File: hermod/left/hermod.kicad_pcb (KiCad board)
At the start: 2 copper layers, 154 x 149.2 mm, 164 parts, among them J1 USB_C_Receptacle_USB2.0, J2 Conn_01x05, J3 USB_C_Receptacle_USB2.0, Q1 AO3401A, Q2 MMUN2233LT1G, U1 STM32F072CBT6, U2 PRTR5V0U2X, U3 XC6206PxxxMR-Regulator_Linear, U4 CR2013-MI2120, U5 TXB0101

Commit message: Finished routing
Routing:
- net GND: track 237.5 -> 233.0 mm
- net col0: track 243.0 -> 242.3 mm

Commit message: Updates
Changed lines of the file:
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@@
 		(fp_arc
 			(start 1.699999 -0.702844)
-			(mid 1.712537 -0.814067)
+			(mid 1.712538 -0.814067)
 			(end 1.749484 -0.919721)
 			(stroke
@@
 		(fp_arc
 			(start 1.749484 0.919719)
-			(mid 1.712534 0.814065)
+			(mid 1.712541 0.814065)
 			(end 1.699999 0.702841)
 			(stroke
@@
 		(fp_arc
 			(start 1.699999 -0.702844)
-			(mid 1.712537 -0.814068)
+			(mid 1.712536 -0.814067)
 			(end 1.749484 -0.919721)
 			(stroke
@@
 		(fp_arc
 			(start 1.749484 0.919719)
-			(mid 1.712517 0.81407)
+			(mid 1.712511 0.81407)
 			(end 1.699999 0.702841)
 			(stroke
@@
 		(fp_arc
 			(start 0.794452 1.499999)
-			(mid 0.925122 1.517375)
+			(mid 0.925123 1.517374)
 			(end 1.046711 1.568298)
 			(stroke
@@
 		(fp_arc
 			(start -1.046711 1.568296)
-			(mid -1.638069 1.504033)
+			(mid -1.638071 1.504032)
 			(end -1.749484 0.919719)
 			(stroke
@@
 		(fp_arc
 			(start 1.749484 0.919719)
-			(mid 1.712534 0.814065)
+			(mid 1.712541 0.814065)
 			(end 1.699999 0.702841)
 			(stroke
@@
 		(fp_arc
 			(start 1.699999 -0.702844)
-			(mid 1.712537 -0.814067)
+			(mid 1.712538 -0.814067)
 			(end 1.749484 -0.919721)
 			(stroke
@@
 		(fp_arc
 			(start 1.699999 -0.702844)
-			(mid 1.712537 -0.814067)
+			(mid 1.712538 -0.814067)
 			(end 1.749484 -0.919721)
 			(stroke
@@
 		(fp_arc
 			(start 1.749484 0.919719)
-			(mid 1.712534 0.814065)
+			(mid 1.712541 0.814065)
 			(end 1.699999 0.702841)
 			(stroke
@@
 		(fp_arc
 			(start 1.749484 0.919719)
-			(mid 1.712534 0.814065)
+			(mid 1.712541 0.814065)
 			(end 1.699999 0.702841)
 			(stroke
@@
 		(fp_arc
 			(start 1.699999 -0.702844)
-			(mid 1.712537 -0.814067)
+			(mid 1.712538 -0.814067)
 			(end 1.749484 -0.919721)
 			(stroke
@@
 		(fp_arc
 			(start 1.749484 0.919719)
-			(mid 1.712534 0.814065)
+			(mid 1.712541 0.814065)
 			(end 1.699999 0.702841)
 			(stroke
@@
 		(fp_arc
 			(start 1.699999 -0.702844)
-			(mid 1.712537 -0.814067)
+			(mid 1.712538 -0.814067)
 			(end 1.749484 -0.919721)
 			(stroke
@@
 		(fp_arc
 			(start 1.699999 -0.702844)
-			(mid 1.712537 -0.814067)
+			(mid 1.712538 -0.814067)
 			(end 1.749484 -0.919721)
 			(stroke
@@
 		(fp_arc
 			(start 1.749484 0.919719)
-			(mid 1.712534 0.814065)
+			(mid 1.712541 0.814065)
 			(end 1.699999 0.702841)
 			(stroke
@@
 		(fp_arc
 			(start 1.749484 0.919719)
-			(mid 1.712534 0.814065)
+			(mid 1.712541 0.814065)
 			(end 1.699999 0.702841)
 			(stroke
@@
 		(fp_arc
 			(start 1.699999 -0.702844)
-			(mid 1.712537 -0.814067)
+			(mid 1.712538 -0.814067)
 			(end 1.749484 -0.919721)
 			(stroke
@@
 		(fp_arc
 			(start 1.699999 -0.702844)
-			(mid 1.712537 -0.814067)
+			(mid 1.712538 -0.814067)
 			(end 1.749484 -0.919721)
 			(stroke
@@
 		(fp_arc
 			(start 1.749484 0.919719)
-			(mid 1.712534 0.814065)
+			(mid 1.712541 0.814065)
 			(end 1.699999 0.702841)
 			(stroke
@@
 		(fp_arc
 			(start 1.699999 -0.702844)
-			(mid 1.712537 -0.814068)
+			(mid 1.712536 -0.814067)
 			(end 1.749484 -0.919721)
 			(stroke
@@
 		(fp_arc
 			(start 1.749484 0.919719)
-			(mid 1.712517 0.81407)
+			(mid 1.712511 0.81407)
 			(end 1.699999 0.702841)
 			(stroke
@@
 		(fp_arc
 			(start 0.794452 1.499999)
-			(mid 0.925122 1.517375)
+			(mid 0.925123 1.517374)
 			(end 1.046711 1.568298)
 			(stroke
@@
 		(fp_arc
 			(start -1.046711 1.568296)
-			(mid -1.638069 1.504033)
+			(mid -1.638071 1.504032)
 			(end -1.749484 0.919719)
 			(stroke
@@
 		(fp_arc
 			(start 1.699999 -0.702844)
-			(mid 1.712537 -0.814067)
+			(mid 1.712538 -0.814067)
 			(end 1.749484 -0.919721)
 			(stroke
@@
 		(fp_arc
 			(start 1.749484 0.919719)
-			(mid 1.712534 0.814065)
+			(mid 1.712541 0.814065)
 			(end 1.699999 0.702841)
 			(stroke
@@
 		(fp_arc
 			(start 1.749484 0.919719)
-			(mid 1.712534 0.814065)
+			(mid 1.712541 0.814065)
 			(end 1.699999 0.702841)
 			(stroke
@@
 		(fp_arc
 			(start 1.699999 -0.702844)
-			(mid 1.712537 -0.814067)
+			(mid 1.712538 -0.814067)
 			(end 1.749484 -0.919721)
 			(stroke
@@
 		(fp_arc
 			(start 1.699999 -0.702844)
-			(mid 1.712537 -0.814067)
+			(mid 1.712538 -0.814067)
 			(end 1.749484 -0.919721)
 			(stroke
@@
 		(fp_arc
 			(start 1.749484 0.919719)
-			(mid 1.712534 0.814065)
+			(mid 1.712541 0.814065)
 			(end 1.699999 0.702841)
 			(stroke
@@
 		(fp_arc
 			(start 1.749484 0.919719)
-			(mid 1.712534 0.814065)
+			(mid 1.712541 0.814065)
 			(end 1.699999 0.702841)
 			(stroke
@@
 		(fp_arc
 			(start 1.699999 -0.702844)
-			(mid 1.712537 -0.814067)
+			(mid 1.712538 -0.814067)
 			(end 1.749484 -0.919721)
 			(stroke
@@
 		(fp_arc
 			(start 1.749484 0.919719)
-			(mid 1.712534 0.814065)
+			(mid 1.712541 0.814065)
 			(end 1.699999 0.702841)
 			(stroke
@@
 		(fp_arc
 			(start 1.699999 -0.702844)
-			(mid 1.712537 -0.814067)
+			(mid 1.712538 -0.814067)
 			(end 1.749484 -0.919721)
 			(stroke
@@
 		(fp_arc
 			(start 1.699999 -0.702844)
-			(mid 1.712537 -0.814067)
+			(mid 1.712538 -0.814067)
 			(end 1.749484 -0.919721)
 			(stroke
@@
 		(fp_arc
 			(start 1.749484 0.919719)
-			(mid 1.712534 0.814065)
+			(mid 1.712541 0.814065)
 			(end 1.699999 0.702841)
 			(stroke
@@
 		(fp_arc
 			(start 1.699999 -0.702844)
-			(mid 1.712537 -0.814067)
+			(mid 1.712538 -0.814067)
 			(end 1.749484 -0.919721)
 			(stroke
@@
 		(fp_arc
 			(start 1.749484 0.919719)
-			(mid 1.712534 0.814065)
+			(mid 1.712541 0.814065)
 			(end 1.699999 0.702841)
 			(stroke
@@
 		(fp_arc
 			(start 1.699999 -0.702844)
-			(mid 1.712537 -0.814067)
+			(mid 1.712538 -0.814067)
 			(end 1.749484 -0.919721)
 			(stroke
@@
 		(fp_arc
 			(start 1.749484 0.919719)
-			(mid 1.712534 0.814065)
+			(mid 1.712541 0.814065)
 			(end 1.699999 0.702841)
 			(stroke
@@
 		(fp_arc
 			(start 1.699999 -0.702844)
-			(mid 1.712537 -0.814067)
+			(mid 1.712538 -0.814067)
 			(end 1.749484 -0.919721)
 			(stroke
@@
 		(fp_arc
 			(start 1.749484 0.919719)
-			(mid 1.712534 0.814065)
+			(mid 1.712541 0.814065)
 			(end 1.699999 0.702841)
 			(stroke
@@
 		(fp_arc
 			(start 1.699999 -0.702844)
-			(mid 1.712537 -0.814067)
+			(mid 1.712538 -0.814067)
 			(end 1.749484 -0.919721)
 			(stroke
@@
 		(fp_arc
 			(start 1.749484 0.919719)
-			(mid 1.712534 0.814065)
+			(mid 1.712541 0.814065)
 			(end 1.699999 0.702841)
 			(stroke
@@
 		(fp_arc
 			(start 1.699999 -0.702844)
-			(mid 1.712537 -0.814067)
+			(mid 1.712538 -0.814067)
 			(end 1.749484 -0.919721)
 			(stroke
@@
 		(fp_arc
 			(start 1.749484 0.919719)
-			(mid 1.712534 0.814065)
+			(mid 1.712541 0.814065)
 			(end 1.699999 0.702841)
 			(stroke
@@
 		(fp_arc
 			(start 1.699999 -0.702844)
-			(mid 1.712537 -0.814067)
+			(mid 1.712538 -0.814067)
 			(end 1.749484 -0.919721)
 			(stroke
@@
 		(fp_arc
 			(start 1.749484 0.919719)
-			(mid 1.712534 0.814065)
+			(mid 1.712541 0.814065)
 			(end 1.699999 0.702841)
 			(stroke
@@
 		(fp_arc
 			(start 1.749484 0.919719)
-			(mid 1.712534 0.814065)
+			(mid 1.712541 0.814065)
 			(end 1.699999 0.702841)
 			(stroke
@@
 		(fp_arc
 			(start 1.699999 -0.702844)
-			(mid 1.712537 -0.814067)
+			(mid 1.712538 -0.814067)
 			(end 1.749484 -0.919721)
 			(stroke
@@
 		(fp_arc
 			(start 1.699999 -0.702844)
-			(mid 1.712537 -0.814067)
+			(mid 1.712538 -0.814067)
 			(end 1.749484 -0.919721)
 			(stroke
@@
 		(fp_arc
 			(start 1.749484 0.919719)
-			(mid 1.712534 0.814065)
+			(mid 1.712541 0.814065)
 			(end 1.699999 0.702841)
 			(stroke
@@
 		(fp_arc
 			(start 1.699999 -0.702844)
-			(mid 1.712537 -0.814067)
+			(mid 1.712538 -0.814067)
 			(end 1.749484 -0.919721)
 			(stroke
@@
 		(fp_arc
 			(start 1.749484 0.919719)
-			(mid 1.712534 0.814065)
+			(mid 1.712541 0.814065)
 			(end 1.699999 0.702841)
 			(stroke
@@
 		(fp_arc
 			(start 1.699999 -0.702844)
-			(mid 1.712537 -0.814067)
+			(mid 1.712538 -0.814067)
 			(end 1.749484 -0.919721)
 			(stroke
@@
 		(fp_arc
 			(start 1.749484 0.919719)
-			(mid 1.712534 0.814065)
+			(mid 1.712541 0.814065)
 			(end 1.699999 0.702841)
 			(stroke
@@
 		(fp_arc
 			(start 1.699999 -0.702844)
-			(mid 1.712537 -0.814067)
+			(mid 1.712538 -0.814067)
 			(end 1.749484 -0.919721)
 			(stroke
@@
 		(fp_arc
 			(start 1.749484 0.919719)
-			(mid 1.712534 0.814065)
+			(mid 1.712541 0.814065)
 			(end 1.699999 0.702841)
 			(stroke
@@
 		(fp_arc
 			(start 1.749484 0.919719)
-			(mid 1.712534 0.814065)
+			(mid 1.712541 0.814065)
 			(end 1.699999 0.702841)
 			(stroke
@@
 		(fp_arc
 			(start 1.699999 -0.702844)
-			(mid 1.712537 -0.814067)
+			(mid 1.712538 -0.814067)
 			(end 1.749484 -0.919721)
 			(stroke
@@
 		(fp_arc
 			(start 1.749484 0.919719)
-			(mid 1.712534 0.814065)
+			(mid 1.712541 0.814065)
 			(end 1.699999 0.702841)
 			(stroke
@@
 		(fp_arc
 			(start 1.699999 -0.702844)
-			(mid 1.712537 -0.814067)
+			(mid 1.712538 -0.814067)
 			(end 1.749484 -0.919721)
 			(stroke
@@
 		(fp_arc
 			(start 1.699999 -0.702844)
-			(mid 1.712537 -0.814067)
+			(mid 1.712538 -0.814067)
 			(end 1.749484 -0.919721)
 			(stroke
@@
 		(fp_arc
 			(start 1.749484 0.919719)
-			(mid 1.712534 0.814065)
+			(mid 1.712541 0.814065)
 			(end 1.699999 0.702841)
 			(stroke
@@
 		(fp_arc
 			(start 1.749484 0.919719)
-			(mid 1.712534 0.814065)
+			(mid 1.712541 0.814065)
 			(end 1.699999 0.702841)
 			(stroke
@@
 		(fp_arc
 			(start 1.699999 -0.702844)
-			(mid 1.712537 -0.814067)
+			(mid 1.712538 -0.814067)
 			(end 1.749484 -0.919721)
 			(stroke
@@
 		(fp_arc
 			(start 1.749484 0.919719)
-			(mid 1.712534 0.814065)
+			(mid 1.712541 0.814065)
 			(end 1.699999 0.702841)
 			(stroke
@@
 		(fp_arc
 			(start 1.699999 -0.702844)
-			(mid 1.712537 -0.814067)
+			(mid 1.712538 -0.814067)
 			(end 1.749484 -0.919721)
 			(stroke

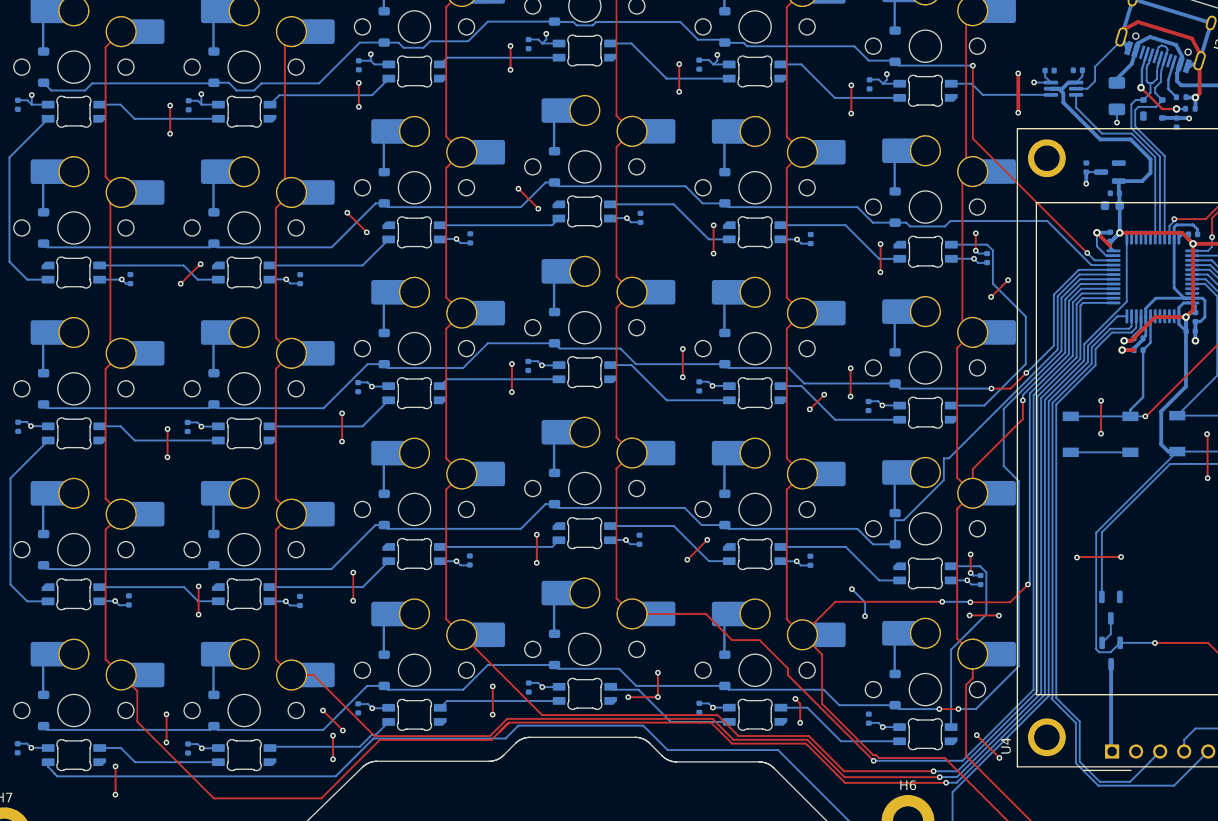
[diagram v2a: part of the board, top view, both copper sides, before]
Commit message: Added PCBWay DRC presets
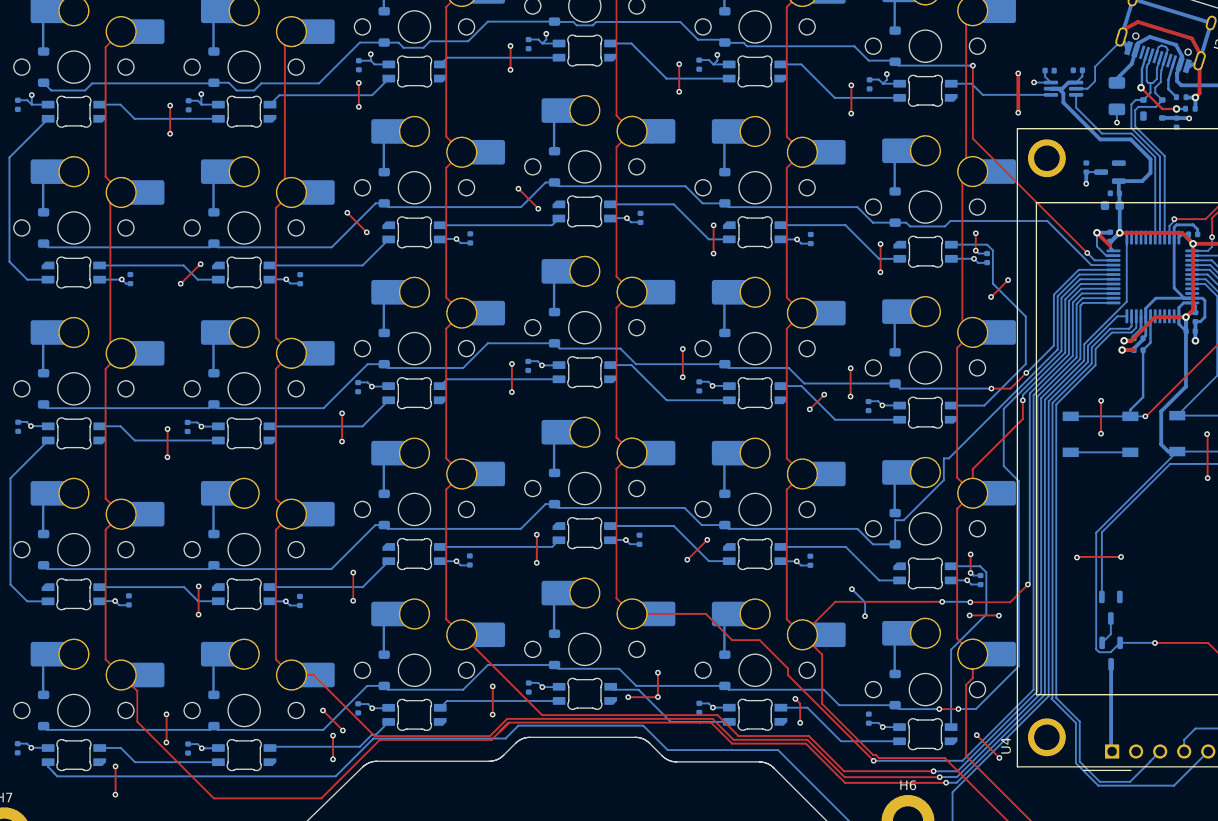
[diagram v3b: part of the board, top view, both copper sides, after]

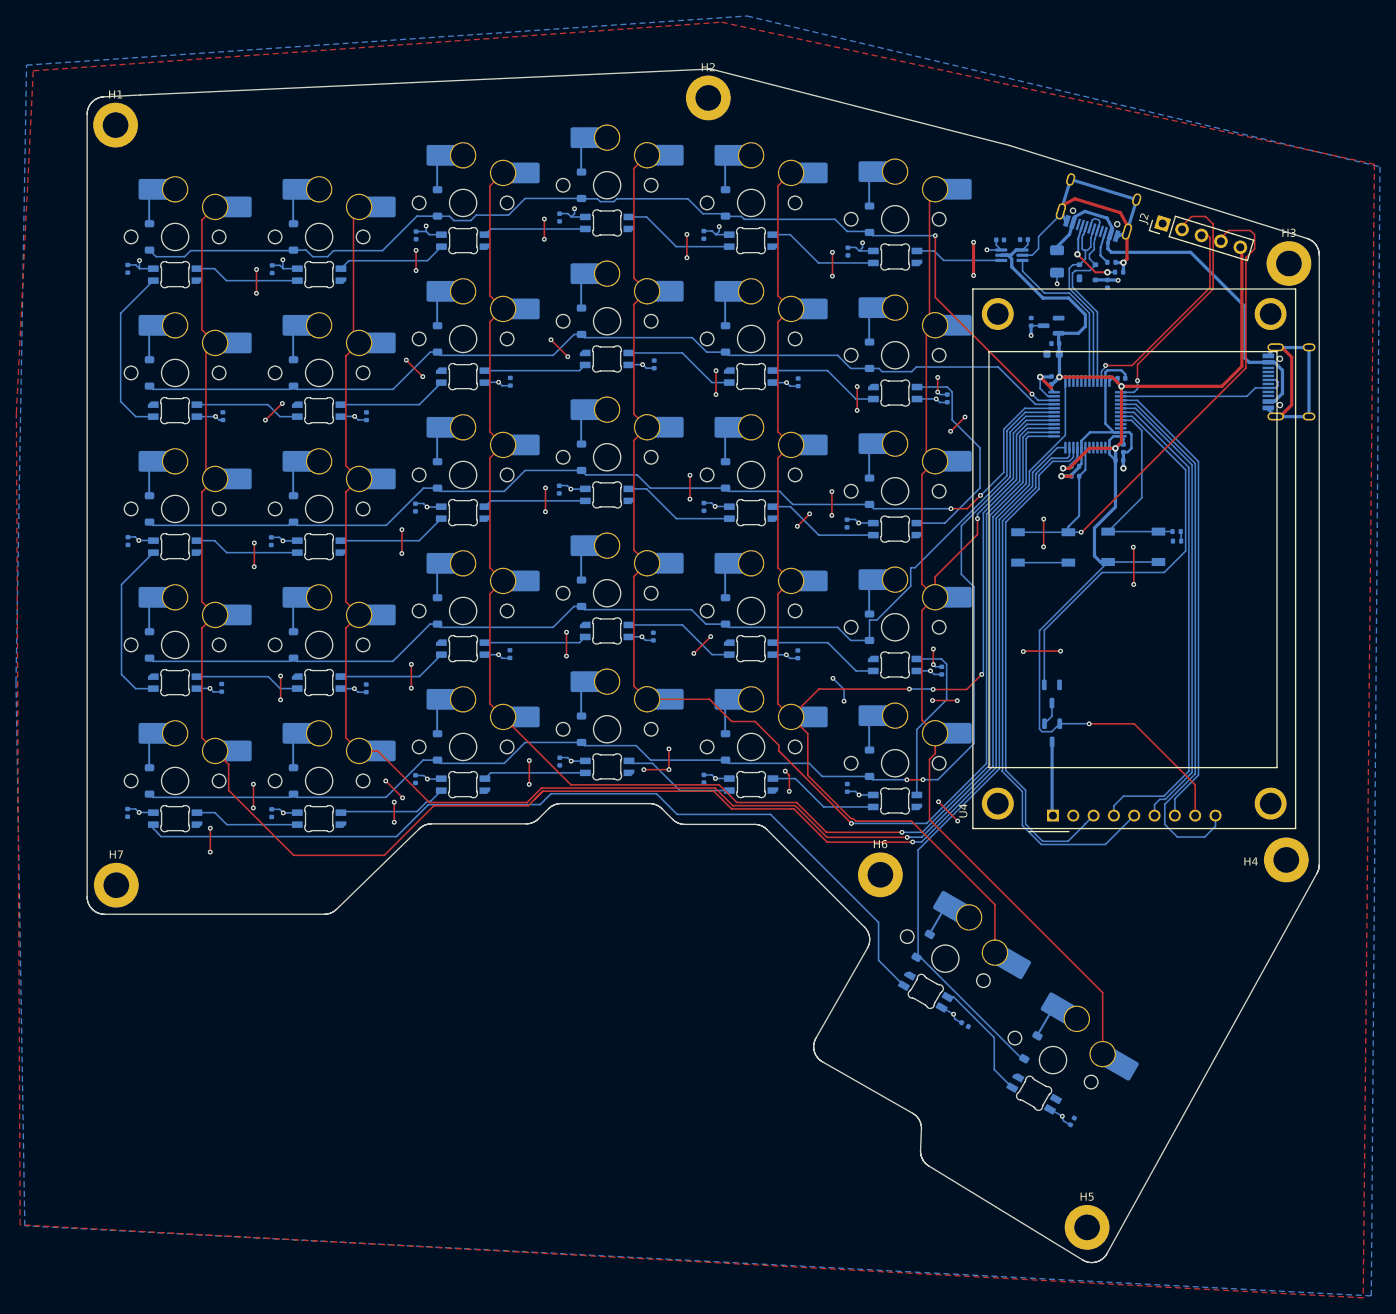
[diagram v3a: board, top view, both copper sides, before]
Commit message: Fixed capacitor orientation
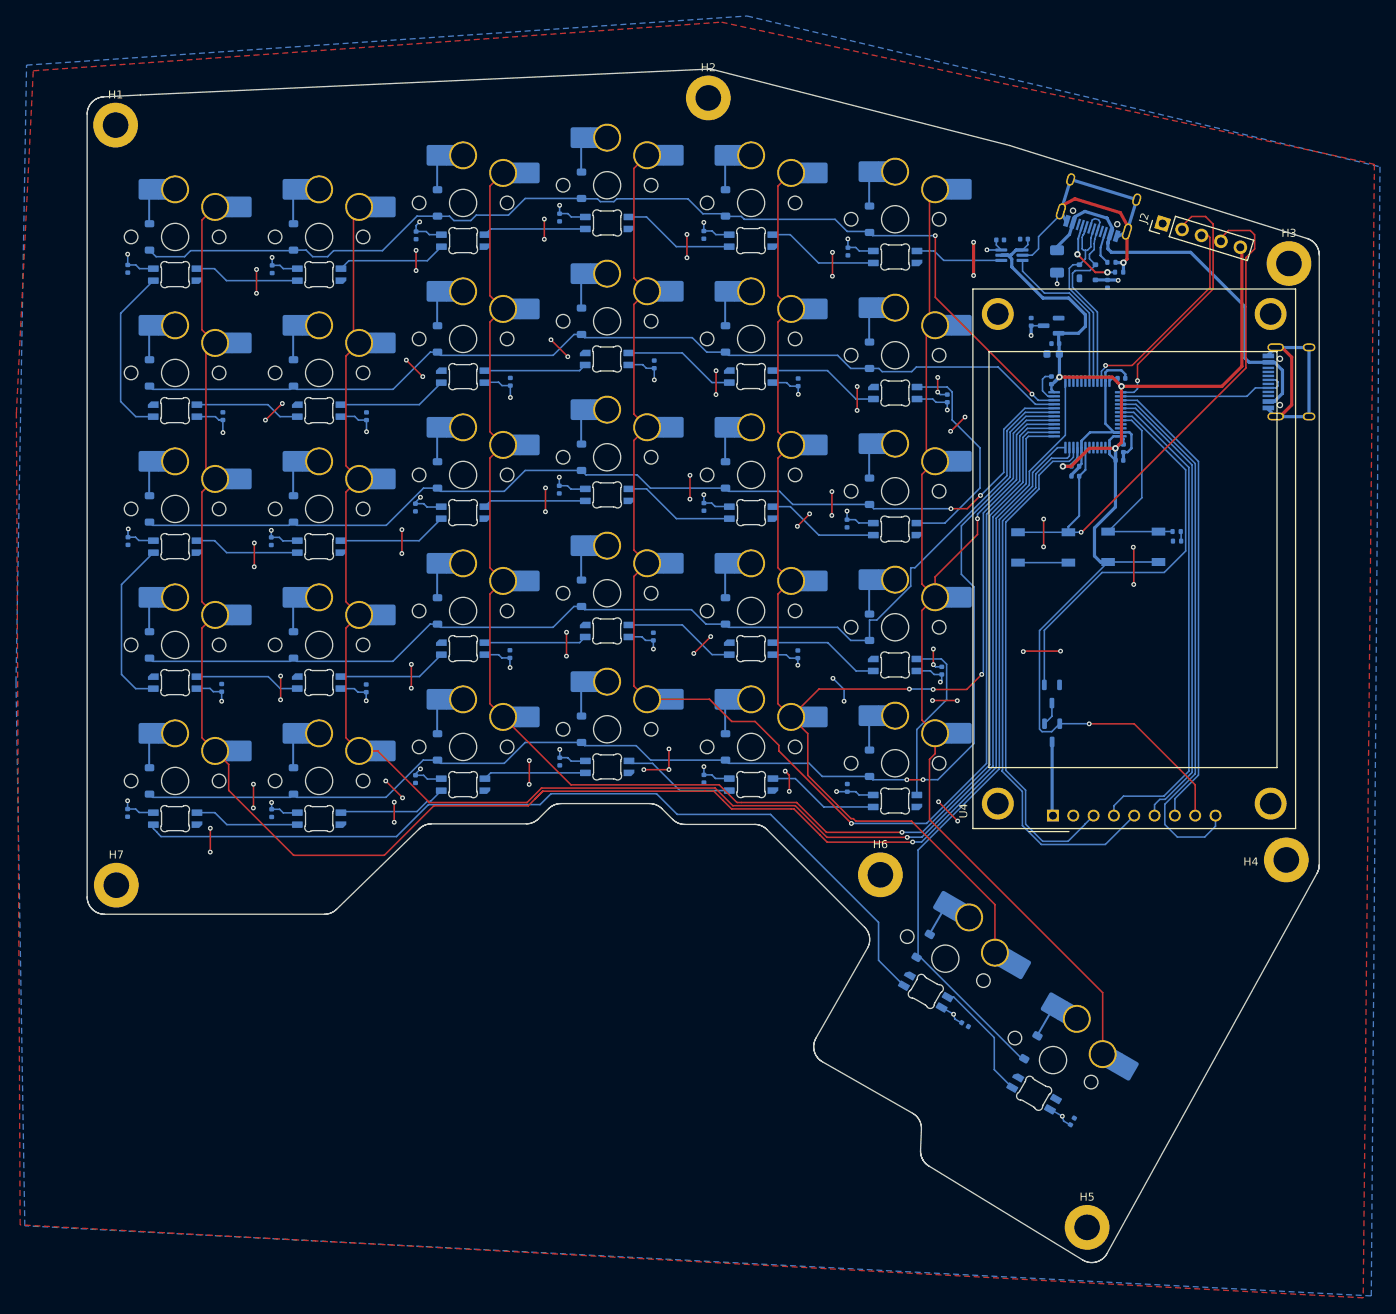
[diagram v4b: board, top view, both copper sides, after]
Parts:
- moved C43 0.06 mm to (152.4, 46.2)
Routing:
- net +5V: track 128.3 -> 156.3 mm
- net GND: track 233.0 -> 227.1 mm, vias 77 -> 74
